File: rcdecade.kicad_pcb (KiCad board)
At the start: 2 copper layers, 63 x 56 mm, 113 parts, among them SW1 SW_Rotary10, SW10 SW_RotaryBCD, SW11 SW_RotaryBCD, SW12 SW_Rotary10, SW13 SW_Rotary10, SW2 SW_RotaryBCD, SW3 SW_RotaryBCD, SW4 SW_Rotary10, SW5 SW_RotaryBCD, SW6 SW_Rotary10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

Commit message: R Decade only
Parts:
- removed C1: 100p, Capacitor_SMD:C_0805_2012Metric
- removed C10, C8, C9: 2n, Capacitor_SMD:C_0805_2012Metric
- removed C11: 3.3n, Capacitor_SMD:C_0805_2012Metric
- removed C12: 4.7n, Capacitor_SMD:C_0805_2012Metric
- removed C13: 10n, Capacitor_SMD:C_0805_2012Metric
- removed C14, C15, C16: 20n, Capacitor_SMD:C_0805_2012Metric
- removed C17: 33nF, Capacitor_SMD:C_0805_2012Metric
- removed C18: 47nF, Capacitor_SMD:C_0805_2012Metric
- removed C19: 100n, Capacitor_SMD:C_0805_2012Metric
- removed C2, C3, C4: 200p, Capacitor_SMD:C_0805_2012Metric
- removed C20, C21, C22: 200n, Capacitor_SMD:C_0805_2012Metric
- removed C23: 330n, Capacitor_SMD:C_0805_2012Metric
- removed C24: 470n, Capacitor_SMD:C_0805_2012Metric
- removed C25, C26, C27: 1u, Capacitor_SMD:C_0805_2012Metric
- removed C28: 1.8u, Capacitor_SMD:C_0805_2012Metric
- removed C29: 2.2u, Capacitor_SMD:C_0805_2012Metric
- removed C30: 3.3u, Capacitor_SMD:C_0805_2012Metric
- removed C31: 4.7u, Capacitor_SMD:C_0805_2012Metric
- removed C32: 10u, Capacitor_SMD:C_0805_2012Metric
- removed C33, C34, C35: 20u, Capacitor_SMD:C_0805_2012Metric
- removed C36: 33u, Capacitor_SMD:C_0805_2012Metric
- removed C37: 47u, Capacitor_SMD:C_0805_2012Metric
- removed C5: 330p, Capacitor_SMD:C_0805_2012Metric
- removed C6: 470p, Capacitor_SMD:C_0805_2012Metric
- removed C7: 1n, Capacitor_SMD:C_0805_2012Metric
- removed SW10, SW11, SW2, SW3, SW5, SW7: SW_RotaryBCD, thumbwheel:Switch_Thumbwheel_BCD
- added J1: Conn_01x01_Female, Connector_Wire:SolderWirePad_1x01_Drill2mm, F.Cu at (124.7, -63.8)
- added J2: Conn_01x01_Female, Connector_Wire:SolderWirePad_1x01_Drill2mm, F.Cu at (124.7, -47.8)
- added LOGO1: dahu-logo, w6ipa-footprints:W6IPA-Logo-9mmx8mm, B.Cu at (124.3, -56.3)
- R11, R13, R15, R17, R20, R22, R24, R26, R29, R31, R33, R35, R38, R40, R42, R44, R47, R49, R51, R53, R56, R58, R60, R62: moved to B.Cu
- moved R12 153.4 mm to (78.3, -64.6), turned to 180 degrees
- moved R21 150.2 mm to (86.5, -64.6), turned to 180 degrees
- moved R31 149.6 mm to (94.3, -64.6), turned to 180 degrees
- moved R19 149.3 mm to (86.5, -61.1), turned to 180 degrees
- moved R49 148.9 mm to (110.3, -64.6), turned to 180 degrees
- moved R29 146.6 mm to (94.3, -58.8), turned to 180 degrees
- moved R57 146.3 mm to (118.5, -64.6), turned to 180 degrees
- moved R38 146.0 mm to (102.5, -58.8), turned to 180 degrees
- moved R11 145.3 mm to (78.3, -58.8), turned to 180 degrees
- moved R48 144.4 mm to (110.3, -64.6), turned to 180 degrees
- moved R39 143.5 mm to (102.5, -64.6), turned to 180 degrees
- moved R58 141.3 mm to (118.5, -64.6), turned to 180 degrees
- moved R13 135.6 mm to (78.3, -64.6), turned to 180 degrees
- moved R47 134.3 mm to (110.3, -58.8), turned to 180 degrees
- moved R22 134.1 mm to (86.5, -64.6), turned to 180 degrees
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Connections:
- net 2 renamed Resistances
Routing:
- net 1: track 275.9 -> 0.00 mm
- net CCommon: track 68.8 -> 0.00 mm
- net Resistances: track 55.9 -> 117.2 mm
- net RCommon: track 48.0 -> 102.6 mm, vias 0 -> 36
- net Net-(R22-Pad2): track 0.00 -> 31.6 mm
- net Net-(R49-Pad2): track 0.00 -> 31.5 mm
- net Net-(R40-Pad2): track 0.00 -> 31.5 mm
- net Net-(R58-Pad2): track 0.00 -> 31.3 mm
- net Net-(R31-Pad2): track 0.00 -> 31.3 mm
- net Net-(R13-Pad2): track 0.00 -> 31.3 mm
- net Net-(R4-Pad2): track 6.68 -> 30.8 mm
- net Net-(R20-Pad2): track 0.00 -> 10.7 mm
- net Net-(R56-Pad2): track 0.00 -> 10.6 mm
- net Net-(R38-Pad2): track 0.00 -> 10.6 mm
- net Net-(R11-Pad2): track 0.00 -> 10.4 mm
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- added copper zone on B.Cu, net RCommon
- added copper zone on F.Cu, net RCommon
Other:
- board size 63 x 56 mm -> 64 x 26 mm
- net class Default: clearance 0.2 -> 0.1524; trace_width 0.25 -> 0.254
- rule pad_to_mask_clearance: 0.051 -> 0.0508
- rule solder_mask_min_width: 0.25 -> 0.1016
- rule trace_clearance: 0.2 -> 0.1524
- board text added: "(CC) BY-NC-SA"
- board text added: "1"
- board text added: "10"
- board text added: "100"
- board text added: "100K"
- board text added: "10K"
- board text added: "1K"
- board text added: "1M"
- board text added: "W6IPA v1.0"

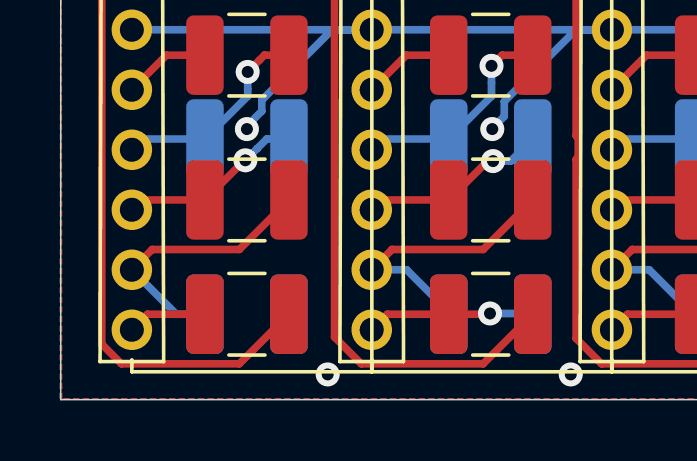
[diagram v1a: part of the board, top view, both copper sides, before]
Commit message: Add missing trace in the x1
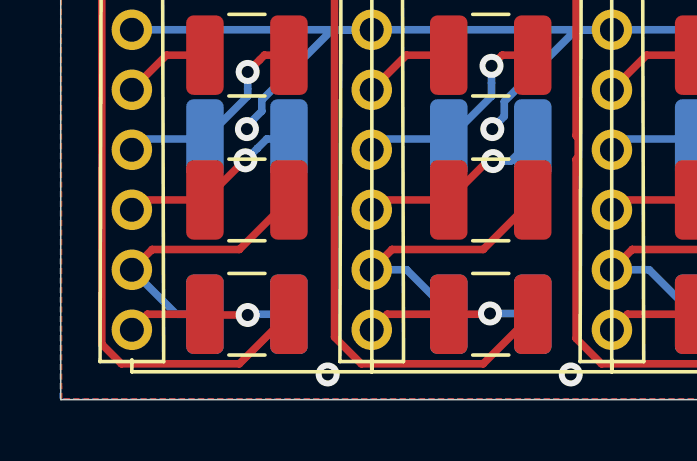
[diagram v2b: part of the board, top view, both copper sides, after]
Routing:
- net Net-(R5-Pad2): track 2.65 -> 5.47 mm, vias 0 -> 1
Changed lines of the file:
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@@
     (thickness 1.6)
     (drawings 13)
-    (tracks 524)
+    (tracks 529)
     (zones 0)
     (modules 73)
@@
   (gr_line (start 128 -69) (end 128 -43) (layer Edge.Cuts) (width 0.05))
   (via (at 70.1802 -58.3946) (size 0.8) (drill 0.4) (layers F.Cu B.Cu) (net 0))
-  (via (at 102.4128 -52.0192) (size 0.8) (drill 0.4) (layers F.Cu B.Cu) (net 64))
-  (via (at 86.5378 -52.0192) (size 0.8) (drill 0.4) (layers F.Cu B.Cu) (net 64))
   (segment (start 68.1282 -61.087) (end 66.3702 -59.329) (width 0.254) (layer F.Cu) (net 1))
   (segment (start 68.8056 -61.087) (end 68.1282 -61.087) (width 0.254) (layer F.Cu) (net 1))
@@
   (segment (start 66.8882 -45.847) (end 66.3702 -45.329) (width 0.254) (layer F.Cu) (net 5))
   (segment (start 68.8056 -45.847) (end 66.8882 -45.847) (width 0.254) (layer F.Cu) (net 5))
+  (via (at 70.231 -45.8216) (size 0.8) (drill 0.4) (layers F.Cu B.Cu) (net 5))
+  (segment (start 70.2564 -45.847) (end 70.231 -45.8216) (width 0.254) (layer B.Cu) (net 5))
+  (segment (start 71.6056 -45.847) (end 70.2564 -45.847) (width 0.254) (layer B.Cu) (net 5))
+  (segment (start 68.831 -45.8216) (end 68.8056 -45.847) (width 0.254) (layer F.Cu) (net 5))
+  (segment (start 70.231 -45.8216) (end 68.831 -45.8216) (width 0.254) (layer F.Cu) (net 5))
   (segment (start 67.045199 -48.003999) (end 66.3702 -47.329) (width 0.254) (layer F.Cu) (net 6))
   (segment (start 67.04619 -48.00499) (end 67.045199 -48.003999) (width 0.254) (layer F.Cu) (net 6))
@@
   (segment (start 115.5302 -54.483) (end 114.3762 -53.329) (width 0.254) (layer F.Cu) (net 63))
   (segment (start 117.0656 -54.483) (end 115.5302 -54.483) (width 0.254) (layer F.Cu) (net 63))
+  (via (at 102.4128 -52.0192) (size 0.8) (drill 0.4) (layers F.Cu B.Cu) (net 64))
+  (via (at 86.5378 -52.0192) (size 0.8) (drill 0.4) (layers F.Cu B.Cu) (net 64))
   (segment (start 114.3762 -55.329) (end 106.3752 -55.329) (width 0.254) (layer B.Cu) (net 64))
   (segment (start 105.420606 -55.329) (end 98.3742 -55.329) (width 0.254) (layer B.Cu) (net 64))

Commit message: Fix // serial
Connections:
- R1 pad 1: Resistances -> Net-(R1-Pad1)
- R10 pad 1: Resistances -> Net-(R10-Pad1)
- R19 pad 1: Resistances -> Net-(R19-Pad1)
- R28 pad 1: Resistances -> Net-(R28-Pad1)
- R37 pad 1: Resistances -> Net-(R37-Pad1)
- R46 pad 1: Resistances -> Net-(R46-Pad1)
- SW1 pad 0: Resistances -> Net-(R1-Pad1)
- SW12 pad 0: Resistances -> Net-(R46-Pad1)
- SW12 pad C: RCommon -> Net-(R37-Pad1)
- SW13 pad C: RCommon -> Net-(R46-Pad1)
- SW4 pad 0: Resistances -> Net-(R10-Pad1)
- SW4 pad C: RCommon -> Net-(R1-Pad1)
- SW6 pad 0: Resistances -> Net-(R19-Pad1)
- SW6 pad C: RCommon -> Net-(R10-Pad1)
- SW8 pad 0: Resistances -> Net-(R28-Pad1)
- SW8 pad C: RCommon -> Net-(R19-Pad1)
- SW9 pad 0: Resistances -> Net-(R37-Pad1)
- SW9 pad C: RCommon -> Net-(R28-Pad1)
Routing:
- net RCommon: track 102.6 -> 0.00 mm, vias 36 -> 0
- net Resistances: track 117.2 -> 20.1 mm
- net Net-(R19-Pad1): track 0.00 -> 15.9 mm
- net Net-(R37-Pad1): track 0.00 -> 15.9 mm
- net Net-(R10-Pad1): track 0.00 -> 15.8 mm
- net Net-(R28-Pad1): track 0.00 -> 15.7 mm
- net Net-(R46-Pad1): track 0.00 -> 15.7 mm
- net Net-(R1-Pad1): track 0.00 -> 15.6 mm
- net Net-(R41-Pad2): track 5.70 -> 9.51 mm, vias 1 -> 0
- net Net-(R23-Pad2): track 5.78 -> 9.58 mm, vias 1 -> 0
- net Net-(R32-Pad2): track 5.58 -> 9.25 mm, vias 1 -> 0
- net Net-(R14-Pad2): track 5.60 -> 9.26 mm, vias 1 -> 0
- net Net-(R50-Pad2): track 5.60 -> 9.25 mm, vias 1 -> 0
- net Net-(R59-Pad2): track 5.94 -> 9.51 mm, vias 1 -> 0
- net Net-(R5-Pad2): track 5.47 -> 9.00 mm, vias 1 -> 0
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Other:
- board text added: "W6IPA v1.1"
- board text removed: "W6IPA v1.0"

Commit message: disconnect copper - v1.1
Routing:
- net RCommon: track 0.00 -> 72.5 mm
- added copper zone on B.Cu, net (none)
- added copper zone on F.Cu, net (none)
- removed copper zone on B.Cu, net RCommon
- removed copper zone on F.Cu, net RCommon
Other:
- board size 64 x 26 mm -> 64 x 26.5 mm
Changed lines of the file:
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@@
     (thickness 1.6)
     (drawings 13)
-    (tracks 407)
+    (tracks 413)
     (zones 0)
     (modules 73)
@@
     (effects (font (size 1 1) (thickness 0.15)))
   )
-  (gr_text 100 (at 86.6836 -67.845) (layer F.SilkS)
+  (gr_text 10K (at 86.6836 -67.845) (layer F.SilkS)
     (effects (font (size 1 1) (thickness 0.15)))
   )
-  (gr_text 1M (at 117.6836 -67.845) (layer F.SilkS)
+  (gr_text 1 (at 117.6836 -67.845) (layer F.SilkS)
     (effects (font (size 1 1) (thickness 0.15)))
   )
-  (gr_text 100K (at 110.6836 -67.845) (layer F.SilkS)
+  (gr_text "10\n" (at 110.6836 -67.845) (layer F.SilkS)
     (effects (font (size 1 1) (thickness 0.15)))
   )
-  (gr_text 10K (at 101.6836 -67.845) (layer F.SilkS)
+  (gr_text 100 (at 101.6836 -67.845) (layer F.SilkS)
     (effects (font (size 1 1) (thickness 0.15)))
   )
@@
     (effects (font (size 1 1) (thickness 0.15)))
   )
-  (gr_text 1 (at 69.6836 -67.845) (layer F.SilkS)
+  (gr_text 1M (at 69.6836 -67.845) (layer F.SilkS)
     (effects (font (size 1 1) (thickness 0.15)))
   )
-  (gr_text 10 (at 78.6836 -67.845) (layer F.SilkS)
+  (gr_text "100K\n" (at 78.6836 -67.845) (layer F.SilkS)
     (effects (font (size 1 1) (thickness 0.15)))
   )
   (gr_line (start 64 -69) (end 128 -69) (layer Edge.Cuts) (width 0.05))
-  (gr_line (start 64 -69) (end 64 -43) (layer Edge.Cuts) (width 0.05))
-  (gr_line (start 128 -43) (end 64 -43) (layer Edge.Cuts) (width 0.05))
-  (gr_line (start 128 -69) (end 128 -43) (layer Edge.Cuts) (width 0.05))
+  (gr_line (start 64 -69) (end 64 -42.5) (layer Edge.Cuts) (width 0.05))
+  (gr_line (start 128 -42.5) (end 64 -42.5) (layer Edge.Cuts) (width 0.05))
+  (gr_line (start 128 -69) (end 128 -42.5) (layer Edge.Cuts) (width 0.05))
   (segment (start 67.0476 -59.329) (end 66.3702 -59.329) (width 0.254) (layer F.Cu) (net 1))
   (segment (start 68.8056 -61.087) (end 67.0476 -59.329) (width 0.254) (layer F.Cu) (net 1))
@@
   (segment (start 115.5302 -54.483) (end 114.3762 -53.329) (width 0.254) (layer F.Cu) (net 63))
   (segment (start 117.0656 -54.483) (end 115.5302 -54.483) (width 0.254) (layer F.Cu) (net 63))
+  (segment (start 122.433161 -45.594561) (end 124.6836 -47.845) (width 0.254) (layer B.Cu) (net 64))
+  (segment (start 65.415799 -44.870887) (end 66.776486 -43.5102) (width 0.254) (layer B.Cu) (net 64))
+  (segment (start 120.3488 -43.5102) (end 122.433161 -45.594561) (width 0.254) (layer B.Cu) (net 64))
+  (segment (start 66.776486 -43.5102) (end 120.3488 -43.5102) (width 0.254) (layer B.Cu) (net 64))
+  (segment (start 65.415799 -54.374599) (end 65.415799 -44.870887) (width 0.254) (layer B.Cu) (net 64))
+  (segment (start 66.3702 -55.329) (end 65.415799 -54.374599) (width 0.254) (layer B.Cu) (net 64))
   (segment (start 116.1076 -57.329) (end 114.3762 -57.329) (width 0.254) (layer F.Cu) (net 65))
   (segment (start 119.8656 -61.087) (end 116.1076 -57.329) (width 0.254) (layer F.Cu) (net 65))
@@
   (segment (start 106.9352 -56.769) (end 112.9362 -56.769) (width 0.254) (layer B.Cu) (net 71))
   (segment (start 106.3752 -57.329) (end 106.9352 -56.769) (width 0.254) (layer B.Cu) (net 71))
-  (zone (net 64) (net_name RCommon) (layer B.Cu) (hatch edge 0.508)
+  (zone (net 0) (net_name "") (layer B.Cu) (hatch edge 0.508)
     (connect_pads (clearance 0.254))
     (min_thickness 0.254)
@@
     (polygon
       (pts
-        (xy 64.008 -68.961) (xy 127.9906 -68.9356) (xy 127.9652 -43.0022) (xy 63.9826 -43.0276)
+        (xy 64.008 -68.845) (xy 127.9906 -68.9356) (xy 128.0414 -42.545) (xy 64.0334 -42.5704)
       )
     )
   )
-  (zone (net 64) (net_name RCommon) (layer F.Cu) (hatch edge 0.508)
+  (zone (net 0) (net_name "") (layer F.Cu) (hatch edge 0.508)
     (connect_pads (clearance 0.254))
     (min_thickness 0.254)
@@
     (polygon
       (pts
-        (xy 64.008 -68.9864) (xy 128.0414 -68.961) (xy 127.9906 -43.0276) (xy 64.0334 -43.0276)
+        (xy 64.008 -68.9864) (xy 128.0414 -68.961) (xy 127.9652 -42.545) (xy 63.9826 -42.5196)
       )
     )
